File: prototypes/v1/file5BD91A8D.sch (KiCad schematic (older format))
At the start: 17 parts, among them U10 74LS30, U11 KM684000BLP-7L, U12 KM684000BLP-7L, U13 74LS138, U14 28C256, U15 28C256, U3 74LS04, U4 74LS20, U6 74LS00

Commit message: finish logic
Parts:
- added unit 1 of U13
- added unit 2 of U13
- added unit 3 of U13
- added U14: 74LS00, symbol 74xx:74LS00
- added unit 6 of U2
- added unit 4 of U2
- added unit 5 of U2
- gave numbers to parts that had none: 2
- renumbered U6 to U10, U12 to U11, U13 to U12, U14 to U15, U15 to U16, U3 to U2, U11 to U7, U4 to U8, U10 to U9
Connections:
- net RAM_CS: now also U2.13
- net RAM_UDS: now also U11.22 (~CS)
- net ROM_CS: now also U13.3, U2.9; no longer U15.20 (~CS), U16.20 (~CS)
- net UDS: now also U13.5
- net RAM_LDS: now reaches U7.22 (~CS)
- net RAM_LDS: now also U10.8
- net ROM_LDS: now reaches U10.11
- net ROM_LDS: now also U15.20 (~CS)
- net at U10.12: now also U2.8
- net at U10.13: now also U2.10
- net at U10.10: now also U13.2
- net at U10.9: now also U2.12
- new net: U13.4, U14.1
- new net: U13.6, U14.2
- new net LDS: U13.1, U2.11
- new net ROM_UDS: U14.3, U16.20 (~CS)
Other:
- moved on the sheet: JP1, JP2, JP3, U10B, U10C, U10D, U13D, U13E

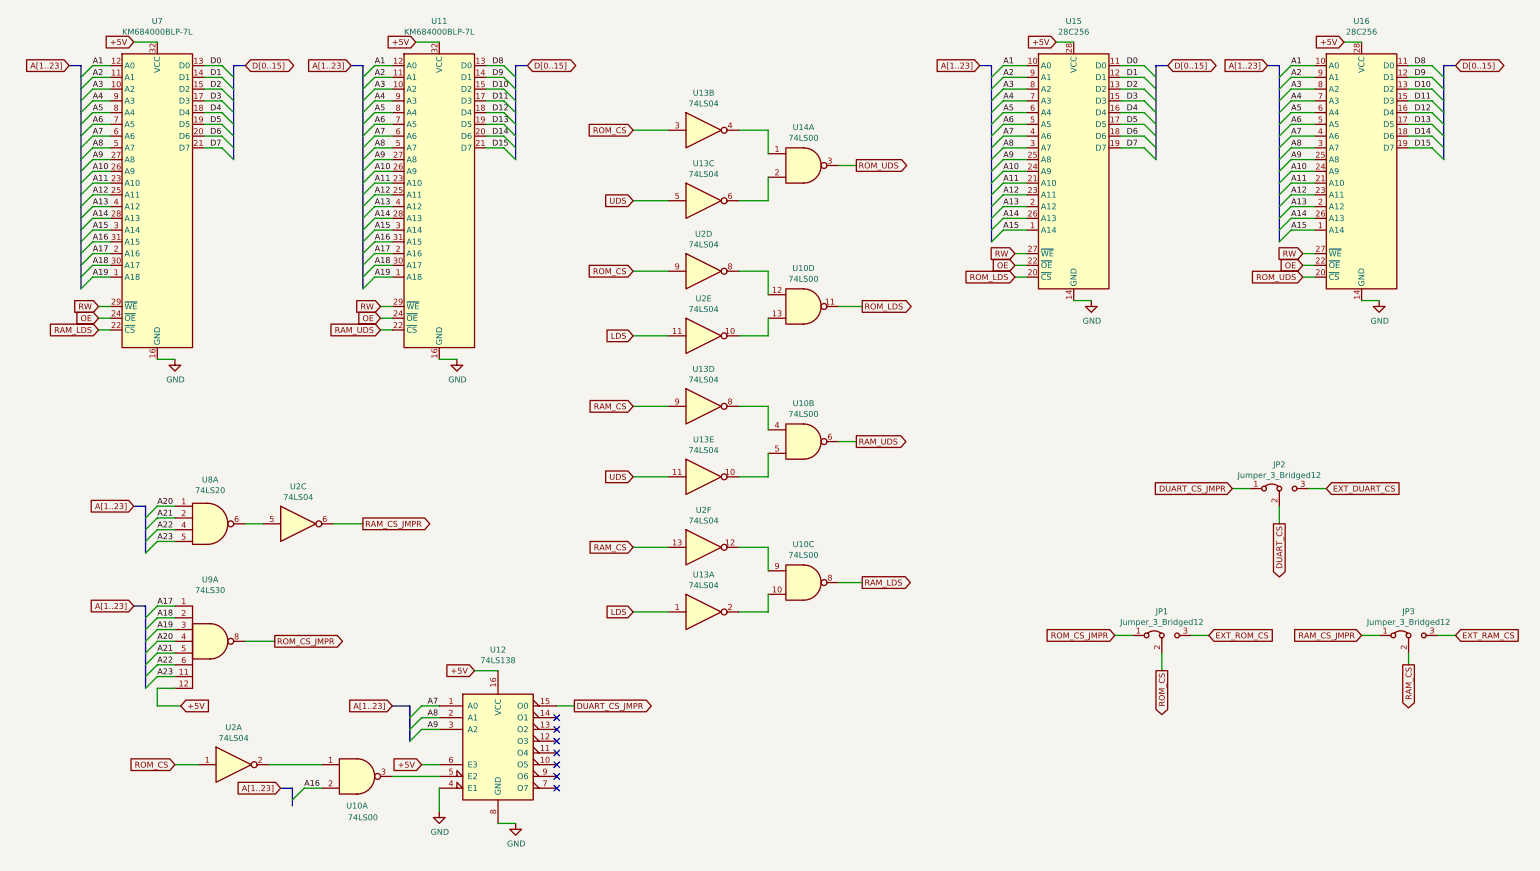
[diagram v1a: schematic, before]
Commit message: optimized logic
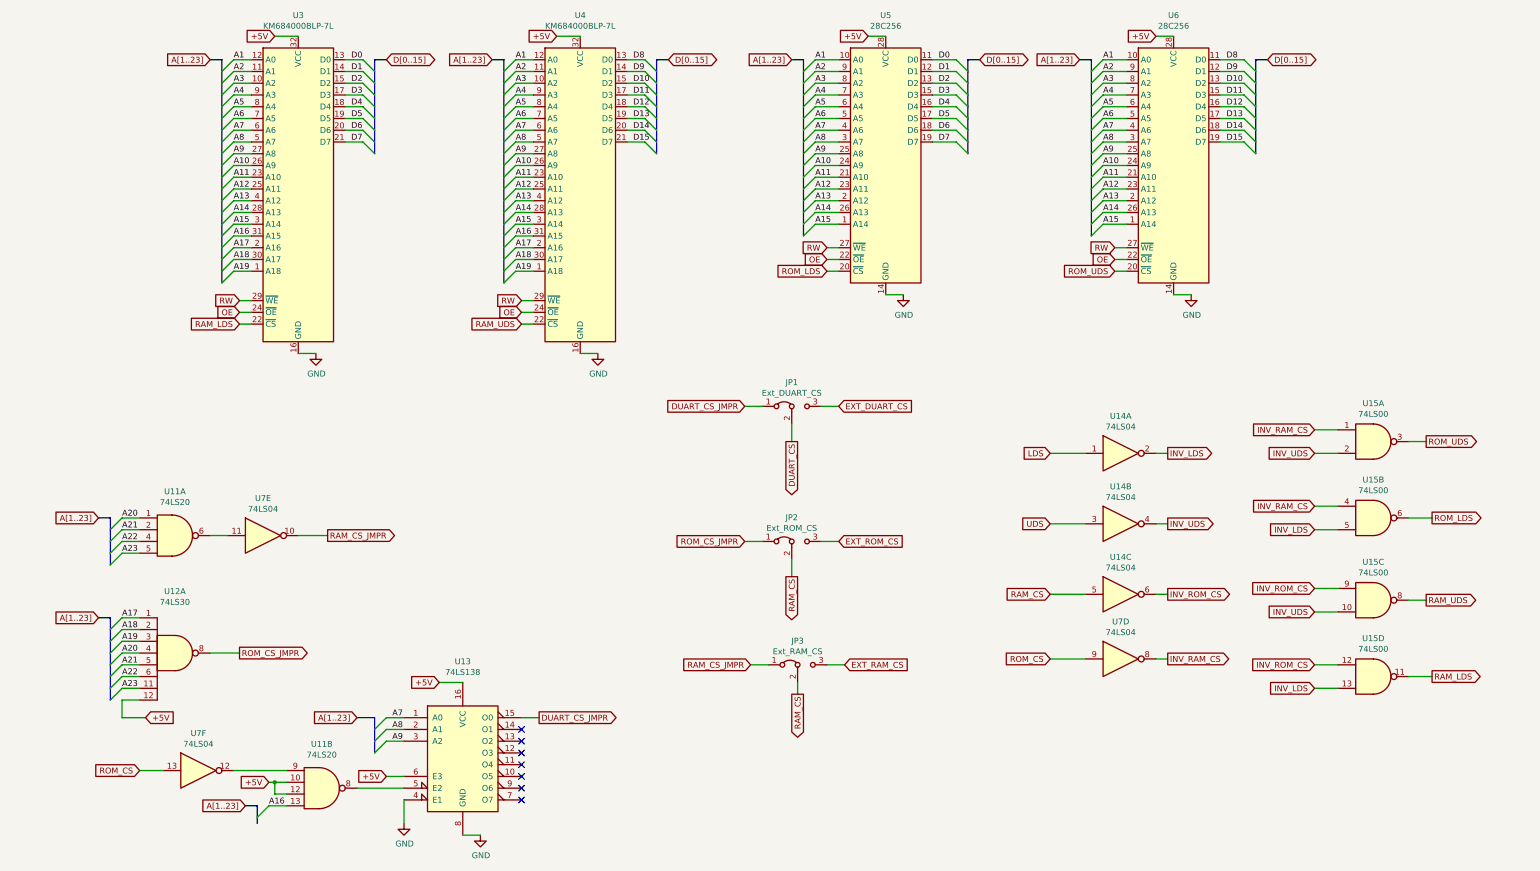
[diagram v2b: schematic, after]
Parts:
- removed unit 1 of U10
- removed unit 1 of U13
- removed unit 4 of U13
- removed unit 5 of U13
- removed unit 6 of U2
- removed unit 4 of U2
- added unit 2 of U11
- added unit 4 of U7
- JP1: renamed from JP2; value Jumper_3_Bridged12 -> Ext_DUART_CS
- JP2: renamed from JP1; value Jumper_3_Bridged12 -> Ext_ROM_CS
- JP3: value Jumper_3_Bridged12 -> Ext_RAM_CS
- U5: renamed from U15; footprint (none) -> Package_DIP:DIP-28_W15.24mm
- U6: renamed from U16; footprint (none) -> Package_DIP:DIP-28_W15.24mm
- renumbered U8 to U11, U9 to U12, U12 to U13, U13 to U14, U2 to U14, U14 to U15, U10 to U15, U7 to U3, U11 to U4, U2 to U7
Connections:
- net +5V: now also U11.10, U11.12
- net A16: now also U11.13
- net LDS: now also U14.1; no longer U14.11
- net RAM_CS: now also JP2.2 (C), U14.5
- net RAM_CS_JMPR: now also U7.10; no longer U7.6
- net RAM_LDS: now also U15.11; no longer U15.8
- net RAM_UDS: now also U15.8; no longer U15.6
- net ROM_CS: now also U7.13, U7.9; no longer JP2.2 (C), U14.3, U7.1
- net ROM_LDS: now also U15.6; no longer U15.11
- net UDS: now also U14.3; no longer U14.5
- net at U13.5 (E2): now also U11.8
- net at U11.6: now also U7.11; no longer U7.5
- net INV_RAM_CS: now reaches U15.1
- net INV_RAM_CS: now also U15.4, U7.8; no longer U14.4
- net INV_UDS: now reaches U15.2
- net INV_UDS: now also U14.4, U15.10; no longer U14.6
- new net: U11.9, U7.12
- new net INV_LDS: U14.2, U15.13, U15.5
- new net INV_ROM_CS: U14.6, U15.12, U15.9
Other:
- moved on the sheet: JP1, JP2, JP3, U11A, U12A, U13, U15A, U3, U4, U5, U6

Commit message: gerbers created, Rev 0 sent to manufacturer
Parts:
- JP1, JP2, JP3: footprint (none) -> Pin_Headers:Pin_Header_Straight_1x03_Pitch2.54mm
- U11, U12, U14, U15, U7: footprint (none) -> Package_DIP:DIP-14_W7.62mm
- U13: footprint (none) -> Package_DIP:DIP-16_W7.62mm
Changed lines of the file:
@@
 F 0 "U12" H 1850 6625 50  0000 C CNN
 F 1 "74LS30" H 1850 6534 50  0000 C CNN
-F 2 "" H 1850 6100 50  0001 C CNN
+F 2 "Package_DIP:DIP-14_W7.62mm" H 1850 6100 50  0001 C CNN
 F 3 "http://www.ti.com/lit/gpn/sn74LS30" H 1850 6100 50  0001 C CNN
 	1    1850 6100
@@
 F 0 "U7" H 2050 7417 50  0000 C CNN
 F 1 "74LS04" H 2050 7326 50  0000 C CNN
-F 2 "" H 2050 7100 50  0001 C CNN
+F 2 "Package_DIP:DIP-14_W7.62mm" H 2050 7100 50  0001 C CNN
 F 3 "http://www.ti.com/lit/gpn/sn74LS04" H 2050 7100 50  0001 C CNN
 	6    2050 7100
@@
 F 0 "U13" H 4300 7728 50  0000 C CNN
 F 1 "74LS138" H 4300 7637 50  0000 C CNN
-F 2 "" H 4300 6950 50  0001 C CNN
+F 2 "Package_DIP:DIP-16_W7.62mm" H 4300 6950 50  0001 C CNN
 F 3 "http://www.ti.com/lit/gpn/sn74LS138" H 4300 6950 50  0001 C CNN
 	1    4300 6950
@@
 F 0 "U11" H 1850 5475 50  0000 C CNN
 F 1 "74LS20" H 1850 5384 50  0000 C CNN
-F 2 "" H 1850 5100 50  0001 C CNN
+F 2 "Package_DIP:DIP-14_W7.62mm" H 1850 5100 50  0001 C CNN
 F 3 "http://www.ti.com/lit/gpn/sn74LS20" H 1850 5100 50  0001 C CNN
 	1    1850 5100
@@
 F 0 "U7" H 2600 5417 50  0000 C CNN
 F 1 "74LS04" H 2600 5326 50  0000 C CNN
-F 2 "" H 2600 5100 50  0001 C CNN
+F 2 "Package_DIP:DIP-14_W7.62mm" H 2600 5100 50  0001 C CNN
 F 3 "http://www.ti.com/lit/gpn/sn74LS04" H 2600 5100 50  0001 C CNN
 	5    2600 5100
@@
 F 0 "JP1" H 7100 4204 50  0000 C CNN
 F 1 "Ext_DUART_CS" H 7100 4113 50  0000 C CNN
-F 2 "" H 7100 4000 50  0001 C CNN
+F 2 "Pin_Headers:Pin_Header_Straight_1x03_Pitch2.54mm" H 7100 4000 50  0001 C CNN
 F 3 "~" H 7100 4000 50  0001 C CNN
 	1    7100 4000
@@
 F 0 "JP3" H 7150 6404 50  0000 C CNN
 F 1 "Ext_RAM_CS" H 7150 6313 50  0000 C CNN
-F 2 "" H 7150 6200 50  0001 C CNN
+F 2 "Pin_Headers:Pin_Header_Straight_1x03_Pitch2.54mm" H 7150 6200 50  0001 C CNN
 F 3 "~" H 7150 6200 50  0001 C CNN
 	1    7150 6200
@@
 F 0 "JP2" H 7100 5354 50  0000 C CNN
 F 1 "Ext_ROM_CS" H 7100 5263 50  0000 C CNN
-F 2 "" H 7100 5150 50  0001 C CNN
+F 2 "Pin_Headers:Pin_Header_Straight_1x03_Pitch2.54mm" H 7100 5150 50  0001 C CNN
 F 3 "~" H 7100 5150 50  0001 C CNN
 	1    7100 5150
@@
 F 0 "U15" H 12050 5975 50  0000 C CNN
 F 1 "74LS00" H 12050 5884 50  0000 C CNN
-F 2 "" H 12050 5650 50  0001 C CNN
+F 2 "Package_DIP:DIP-14_W7.62mm" H 12050 5650 50  0001 C CNN
 F 3 "http://www.ti.com/lit/gpn/sn74ls00" H 12050 5650 50  0001 C CNN
 	3    12050 5650
@@
 F 0 "U15" H 12050 5275 50  0000 C CNN
 F 1 "74LS00" H 12050 5184 50  0000 C CNN
-F 2 "" H 12050 4950 50  0001 C CNN
+F 2 "Package_DIP:DIP-14_W7.62mm" H 12050 4950 50  0001 C CNN
 F 3 "http://www.ti.com/lit/gpn/sn74ls00" H 12050 4950 50  0001 C CNN
 	2    12050 4950
@@
 F 0 "U15" H 12050 6625 50  0000 C CNN
 F 1 "74LS00" H 12050 6534 50  0000 C CNN
-F 2 "" H 12050 6300 50  0001 C CNN
+F 2 "Package_DIP:DIP-14_W7.62mm" H 12050 6300 50  0001 C CNN
 F 3 "http://www.ti.com/lit/gpn/sn74ls00" H 12050 6300 50  0001 C CNN
 	4    12050 6300
@@
 F 0 "U15" H 12050 4625 50  0000 C CNN
 F 1 "74LS00" H 12050 4534 50  0000 C CNN
-F 2 "" H 12050 4300 50  0001 C CNN
+F 2 "Package_DIP:DIP-14_W7.62mm" H 12050 4300 50  0001 C CNN
 F 3 "http://www.ti.com/lit/gpn/sn74ls00" H 12050 4300 50  0001 C CNN
 	1    12050 4300
@@
 F 0 "U14" H 9900 5917 50  0000 C CNN
 F 1 "74LS04" H 9900 5826 50  0000 C CNN
-F 2 "" H 9900 5600 50  0001 C CNN
+F 2 "Package_DIP:DIP-14_W7.62mm" H 9900 5600 50  0001 C CNN
 F 3 "http://www.ti.com/lit/gpn/sn74LS04" H 9900 5600 50  0001 C CNN
 	3    9900 5600
@@
 F 0 "U14" H 9900 5317 50  0000 C CNN
 F 1 "74LS04" H 9900 5226 50  0000 C CNN
-F 2 "" H 9900 5000 50  0001 C CNN
+F 2 "Package_DIP:DIP-14_W7.62mm" H 9900 5000 50  0001 C CNN
 F 3 "http://www.ti.com/lit/gpn/sn74LS04" H 9900 5000 50  0001 C CNN
 	2    9900 5000
@@
 F 0 "U14" H 9900 4717 50  0000 C CNN
 F 1 "74LS04" H 9900 4626 50  0000 C CNN
-F 2 "" H 9900 4400 50  0001 C CNN
+F 2 "Package_DIP:DIP-14_W7.62mm" H 9900 4400 50  0001 C CNN
 F 3 "http://www.ti.com/lit/gpn/sn74LS04" H 9900 4400 50  0001 C CNN
 	1    9900 4400
@@
 F 0 "U7" H 9900 6467 50  0000 C CNN
 F 1 "74LS04" H 9900 6376 50  0000 C CNN
-F 2 "" H 9900 6150 50  0001 C CNN
+F 2 "Package_DIP:DIP-14_W7.62mm" H 9900 6150 50  0001 C CNN
 F 3 "http://www.ti.com/lit/gpn/sn74LS04" H 9900 6150 50  0001 C CNN
 	4    9900 6150
@@
 F 0 "U11" H 3100 7625 50  0000 C CNN
 F 1 "74LS20" H 3100 7534 50  0000 C CNN
-F 2 "" H 3100 7250 50  0001 C CNN
+F 2 "Package_DIP:DIP-14_W7.62mm" H 3100 7250 50  0001 C CNN
 F 3 "http://www.ti.com/lit/gpn/sn74LS20" H 3100 7250 50  0001 C CNN
 	2    3100 7250
